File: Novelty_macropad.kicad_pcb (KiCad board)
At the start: 2 copper layers, 100 x 59 mm, 54 parts, among them J2 Conn_01x07, J3 Conn_01x06, SW1 SW_Push, SW10 SW_Push, SW11 SW_Push, SW2 SW_Push, SW3 SW_Push, SW4 SW_Push, SW5 SW_Push, SW6 SW_Push, SW7 SW_Push, SW8 SW_Push, SW9 SW_Push, U2 ATmega32U4, X1 XRCGB16M000FXN00R0

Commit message: plate added, step files
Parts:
- added H1: MountingHole, MountingHole:MountingHole_2.7mm_M2.5, F.Cu at (108.5, 140.1)
- added H2: MountingHole, MountingHole:MountingHole_2.7mm_M2.5, F.Cu at (200.5, 140.1)
- added H3: MountingHole, MountingHole:MountingHole_2.7mm_M2.5, F.Cu at (160.7, 87.8)
- LED_2: value STATUS_LED -> STS_LED
- moved D3 2.90 mm to (160.0, 98.7)
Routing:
- net Row0: track 168.2 -> 169.3 mm
- net Col2: track 91.3 -> 91.9 mm
- net Col1: track 100.2 -> 100.8 mm
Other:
- board text added: "Col0"
- board text added: "Col1"
- board text added: "Col2"
- board text added: "Col3"
- board text added: "Col4"
- board text added: "Row0"
- board text added: "Row1"

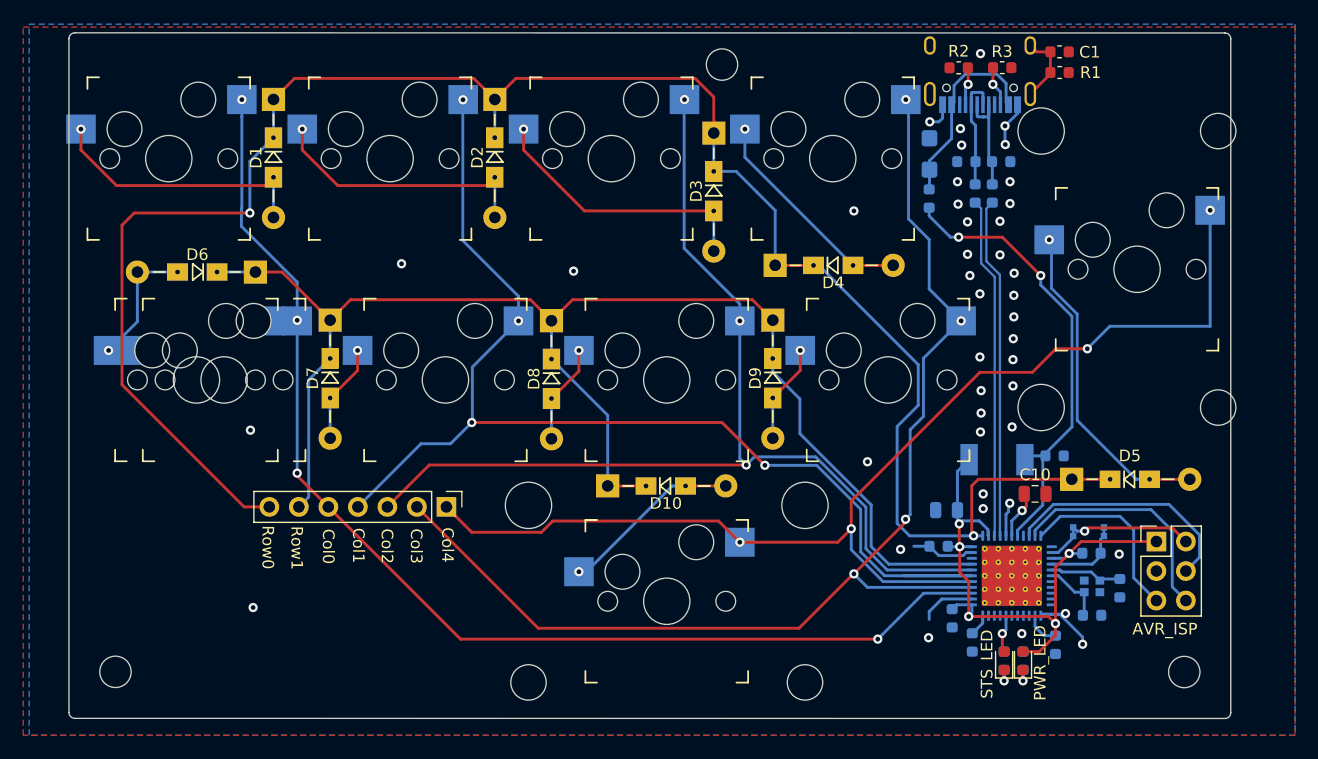
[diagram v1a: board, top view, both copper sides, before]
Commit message: Corrected silkscreen and markings
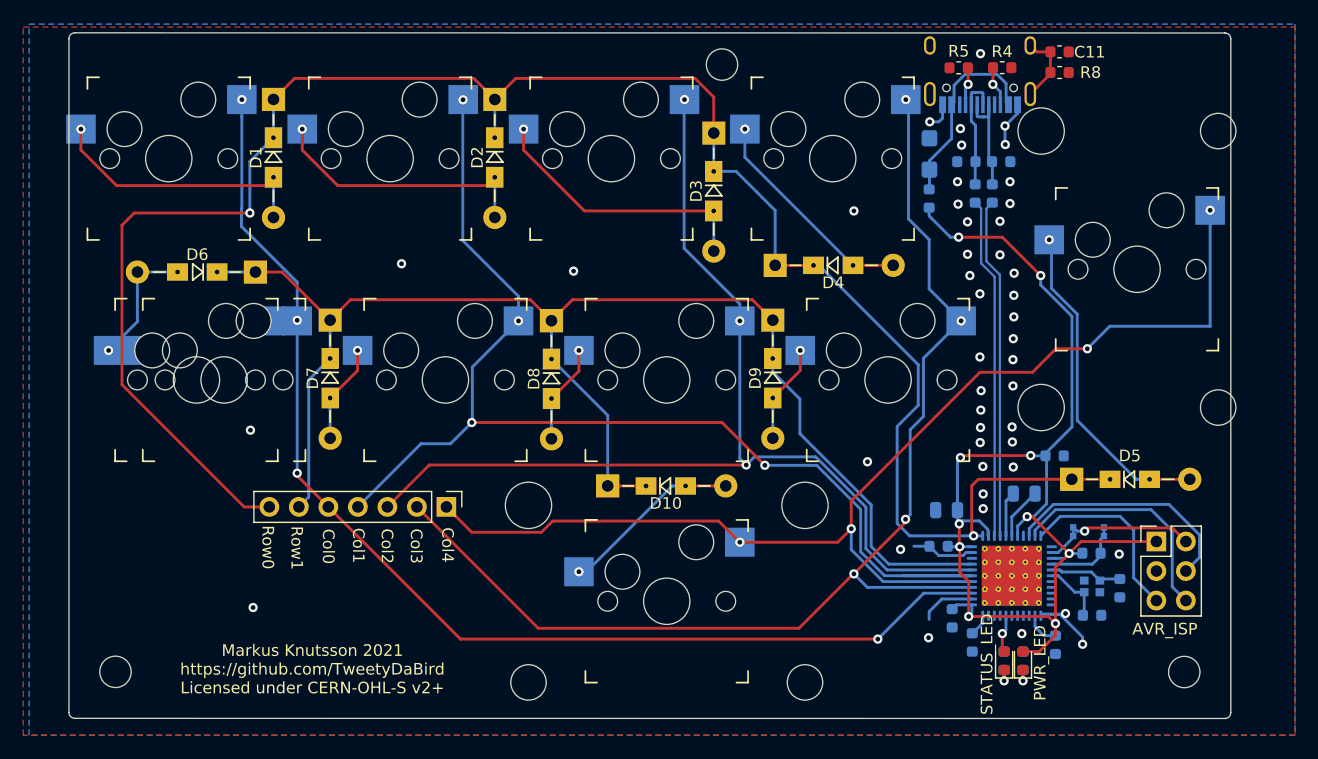
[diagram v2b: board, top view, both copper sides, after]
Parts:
- removed ZD1: SM5817-W, Diode_SMD:D_MELF
- C3: renamed from C10; moved to B.Cu
- LED_1: renamed from LED_2; value STS_LED -> STATUS_LED
- moved C3 0.94 mm to (186.7, 124.7), turned to 180 degrees
- renumbered C5 to C1, C3 to C10, C1 to C11, C6 to C2, C12 to C4, C2 to C5, C4 to C6, C11 to C9, J2 to J1, J3 to J2, LED_1 to LED_2, R7 to R1, R4 to R2, R5 to R3, R3 to R4, R2 to R5, R11 to R6, R13 to R7, R1 to R8, S2 to S1, SW9 to SW10, SW10 to SW11, SW11 to SW7, SW7 to SW8, SW8 to SW9, U2 to U1
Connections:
- net /Sheet60039BC7/BOOT renamed /BOOT
- net /Sheet60039BC7/DD+ renamed /DD+
- net /Sheet60039BC7/DD- renamed /DD-
- net /Sheet60039BC7/LED renamed /LED
- net /Sheet60039BC7/UCAP renamed /UCAP
- net /Sheet60039BC7/XTAL1 renamed /XTAL1
- net /Sheet60039BC7/XTAL2 renamed /XTAL2
- C4 pad 1: VBUS -> VCC
- F1 pad 1: VBUS -> VCC
- U1 pad 7: VBUS -> VCC
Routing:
- net VCC: track 56.3 -> 106.8 mm, vias 5 -> 10
- net VBUS: track 39.8 -> 0.00 mm, vias 2 -> 0
- net GND: track 34.2 -> 35.1 mm, vias 42 -> 45
- net /UCAP: track 4.09 -> 4.46 mm, vias 1 -> 0
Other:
- board text added: "Markus Knutsson 2021 https://github.com/TweetyDaBird Licensed under CERN-OHL-S v2+"
